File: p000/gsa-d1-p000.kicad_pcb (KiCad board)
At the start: 2 copper layers, 99.7 x 33 mm, 36 parts, among them J401 CONN-3, J402 CONN-2, J403 CONN-3, J404 CONN-2, U401 LM1876

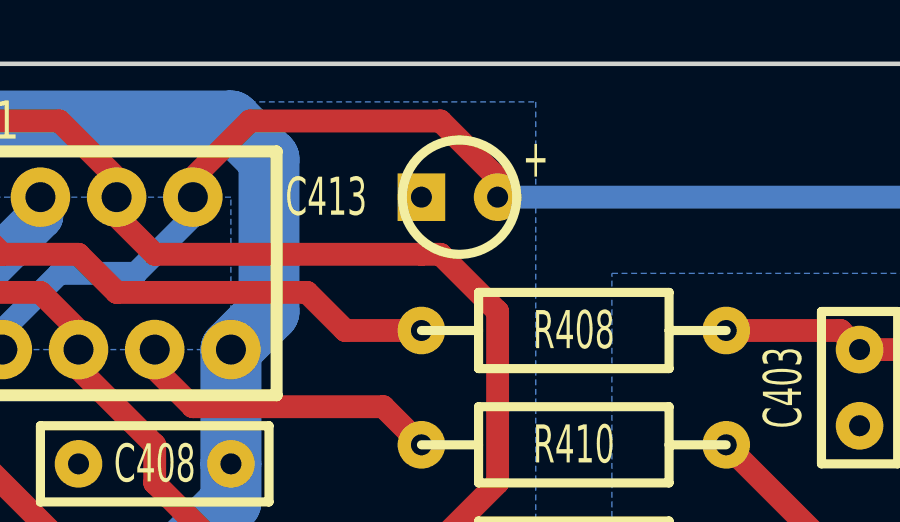
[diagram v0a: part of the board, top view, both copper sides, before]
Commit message: Reduce size of power supply PCB
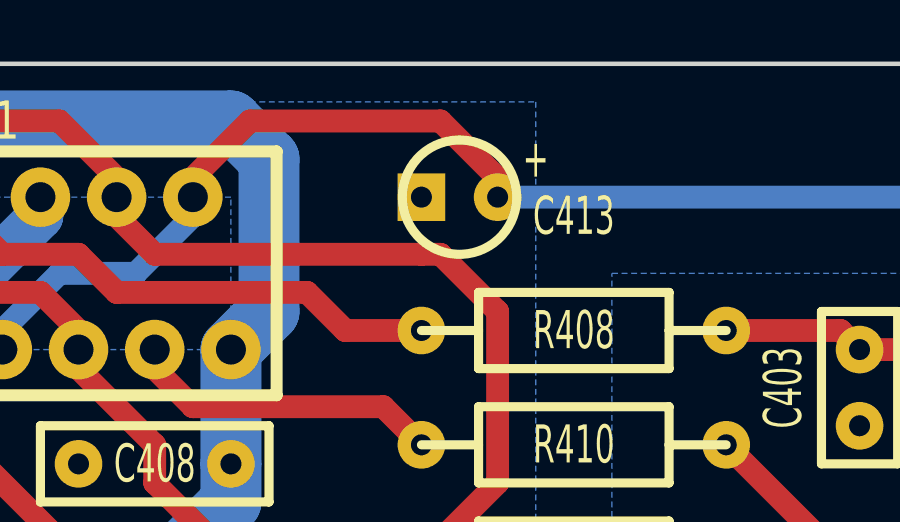
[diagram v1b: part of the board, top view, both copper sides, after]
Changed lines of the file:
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@@
     (links 61)
     (no_connects 0)
-    (area 93.904999 81.006999 193.750001 115.61125)
+    (area 93.904999 81.204999 193.750001 114.375001)
     (thickness 1.6)
     (drawings 18)
@@
   (module gsa:ELEC4R (layer F.Cu)
     (at 156.845 85.725 180)
-    (fp_text reference C413 (at 4.445 0 360) (layer F.SilkS)
-      (effects (font (size 1.27 0.762) (thickness 0.1905)))
-    )
+    (fp_text reference C413 (at -3.81 -0.635 360) (layer F.SilkS)
+      (effects (font (size 1.27 0.762) (thickness 0.1905)))
+    )

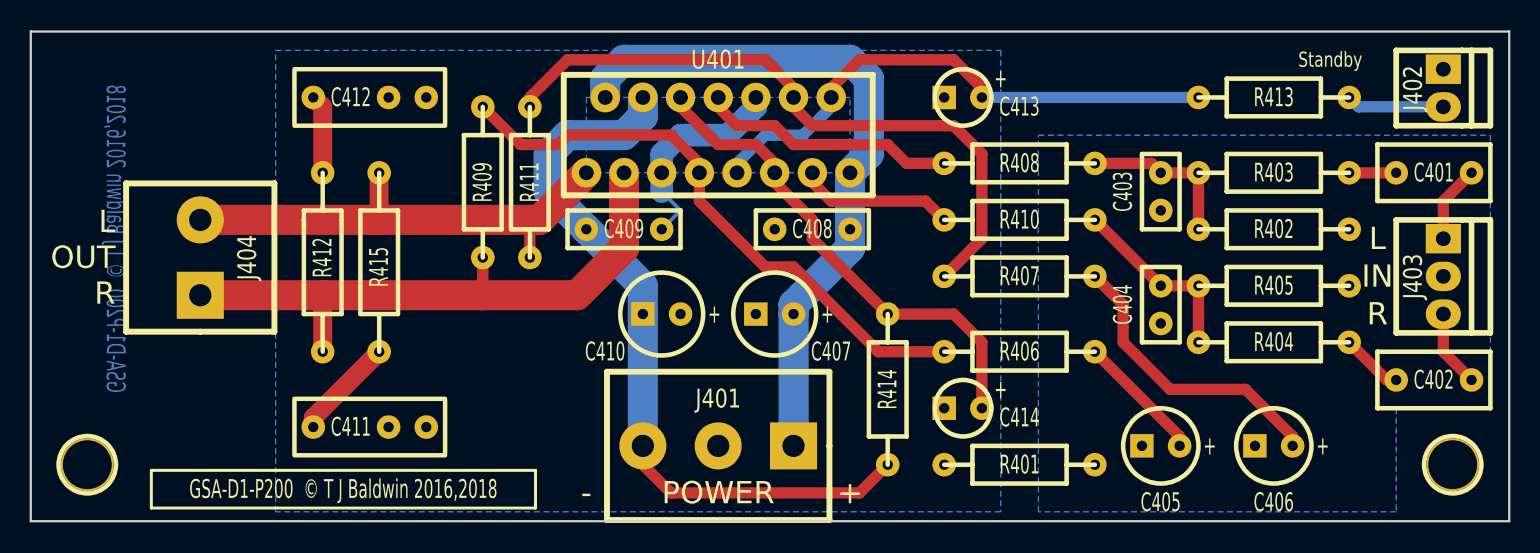
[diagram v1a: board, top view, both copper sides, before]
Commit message: Updated to use KiCad v5
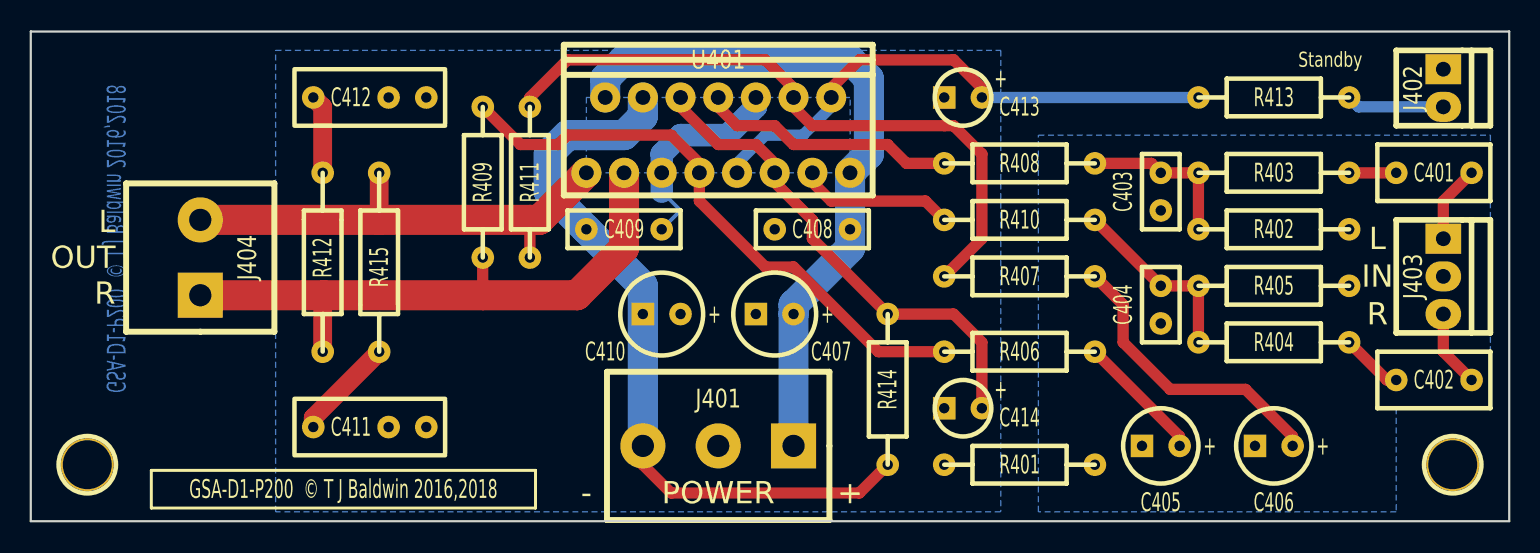
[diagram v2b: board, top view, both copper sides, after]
